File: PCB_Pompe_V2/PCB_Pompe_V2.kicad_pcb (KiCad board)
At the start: 2 copper layers, 199 parts, among them J1 Conn_01x04_Female, J10 Conn_01x03_Female, J11 Conn_01x03_Female, J12 Conn_01x03_Female, J13 Conn_01x05_Female, J14 Conn_01x03_Female, J15 Conn_01x03_Female, J16 Conn_01x03_Female, J17 Conn_01x03_Female, J18 Conn_01x03_Female, J19 Conn_01x03_Female, J2 Conn_01x04_Female, J3 Conn_01x03_Female, J4 Conn_01x03_Female, J5 Conn_01x03_Female, J6 Conn_01x03_Female, J7 Conn_01x03_Female, J8 Conn_01x02_Male, J9 Conn_01x03_Female, Q1 DMN10H700S, Q10 DMN10H700S, Q11 DMN10H700S, Q12 DMN10H700S, Q13 DMN10H700S, Q14 DMN10H700S, Q15 DMN10H700S, Q16 DMN10H700S, Q17 DMN10H700S, Q18 DMN10H700S, Q19 DMN10H700S, Q2 DMN10H700S, Q20 DMN10H700S, Q21 DMN10H700S, Q22 DMN10H700S, Q23 DMN10H700S, Q24 DMN10H700S, Q25 DMN10H700S, Q26 DMN10H700S, Q27 DMN10H700S, Q28 DMN10H700S, Q29 DMN10H700S, Q3 DMN10H700S, Q30 DMN10H700S, Q4 DMN10H700S, Q5 DMN10H700S, Q6 DMN10H700S, Q7 DMN10H700S, Q8 DMN10H700S, Q9 DMN10H700S, SW1 SW_Push, U1 SN65HVD232, U2 STM32F302C6Tx, U3 NCP1117-3.3_SOT223, Y1 8MHz

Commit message: change connector and some final touch
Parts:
- moved J8 120.9 mm to (184.2, 97.2), turned to 270 degrees
- moved H2 115.8 mm to (186.8, 129.8)
- moved C10 110.1 mm to (173.5, 100.0), turned to 90 degrees
- moved J13 104.0 mm to (158.5, 92.5), turned to 90 degrees
- moved R26 101.8 mm to (165.2, 76.5), turned to 270 degrees
- moved D26 98.1 mm to (165.2, 80.2), turned to 270 degrees
- moved J9 94.8 mm to (159.3, 78.0), turned to 180 degrees
- moved D28 94.6 mm to (157.0, 82.5), turned to 180 degrees
- moved D27 93.8 mm to (153.5, 80.5), turned to 270 degrees
- moved R51 92.7 mm to (181.5, 131.5), turned to 90 degrees
- moved Q11 90.2 mm to (162.5, 85.8), turned to 180 degrees
- moved R31 89.0 mm to (127.5, 118.5), turned to 90 degrees
- moved R50 88.1 mm to (169.8, 131.5), turned to 90 degrees
- moved J16 88.0 mm to (175.5, 130.0)
- moved D25 87.8 mm to (161.8, 82.5), turned to 180 degrees
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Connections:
- Y1 pad 1: Net-(C1-Pad1) -> Net-(C2-Pad1)
- Y1 pad 3: GND -> Net-(C1-Pad1)
- Y1 pad 4: Net-(C2-Pad1) -> GND
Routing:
- net +3V3: track 0.00 -> 125.4 mm
- net CANH: track 0.00 -> 62.7 mm
- net P1: track 0.00 -> 53.4 mm, vias 0 -> 2
- net P8: track 0.00 -> 49.5 mm, vias 0 -> 2
- net V1: track 0.00 -> 47.6 mm, vias 0 -> 2
- net V10: track 0.00 -> 45.0 mm, vias 0 -> 2
- net CANL: track 0.00 -> 41.0 mm, vias 0 -> 2
- net P10: track 0.00 -> 39.4 mm, vias 0 -> 2
- net P14: track 0.00 -> 39.0 mm
- net P2: track 0.00 -> 38.9 mm, vias 0 -> 2
- net V12: track 0.00 -> 38.1 mm, vias 0 -> 2
- net V6: track 0.00 -> 35.4 mm
- net +5V: track 0.00 -> 35.2 mm
- net V2: track 0.00 -> 34.2 mm, vias 0 -> 2
- net V3: track 0.00 -> 34.1 mm, vias 0 -> 2
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- added copper zone on F.Cu, net +5VP
- added copper zone on In1.Cu, net +5VP
- added copper zone on B.Cu, net GND
- added copper zone on F.Cu, net GND
- added copper zone on In2.Cu, net GND
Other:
- board outline added: 89.8 x 59.2 mm
- copper layers 2 -> 4

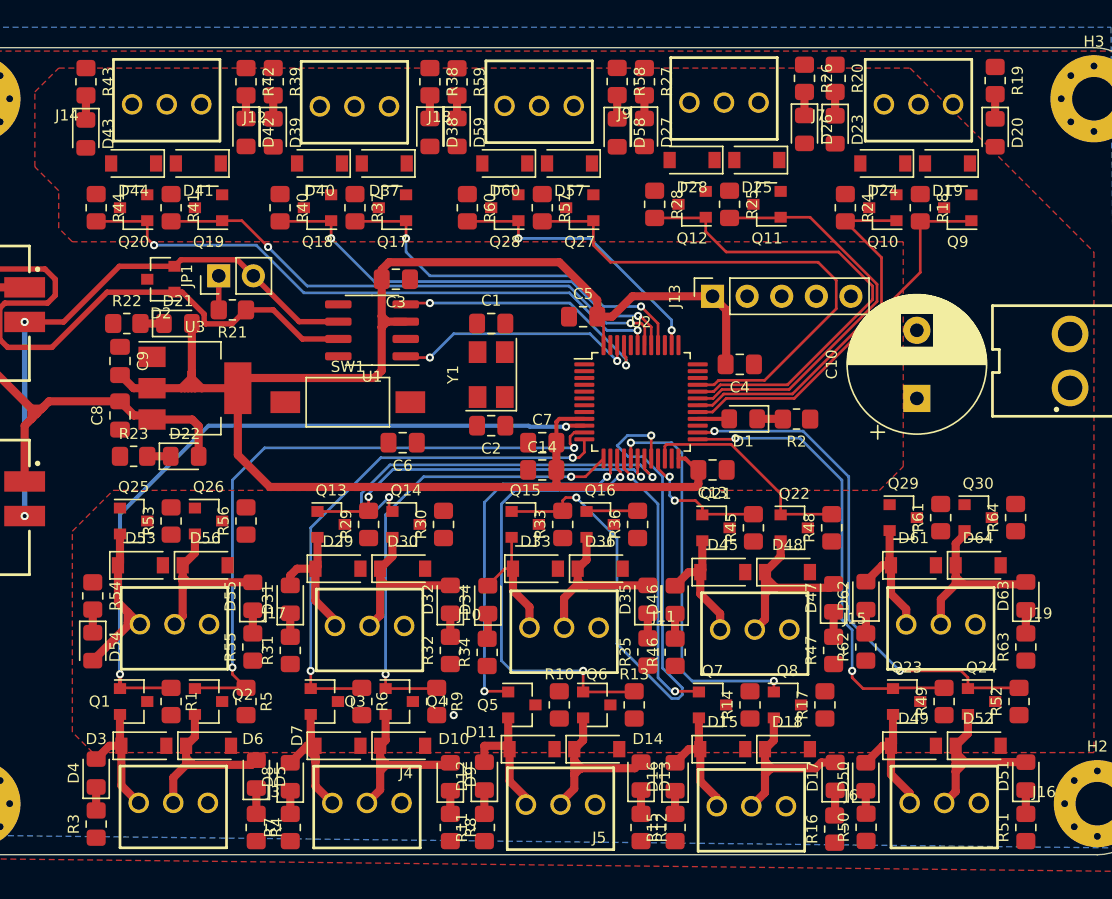
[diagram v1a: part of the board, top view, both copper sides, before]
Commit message: esp32 pas fini + silkscreen  IO ok
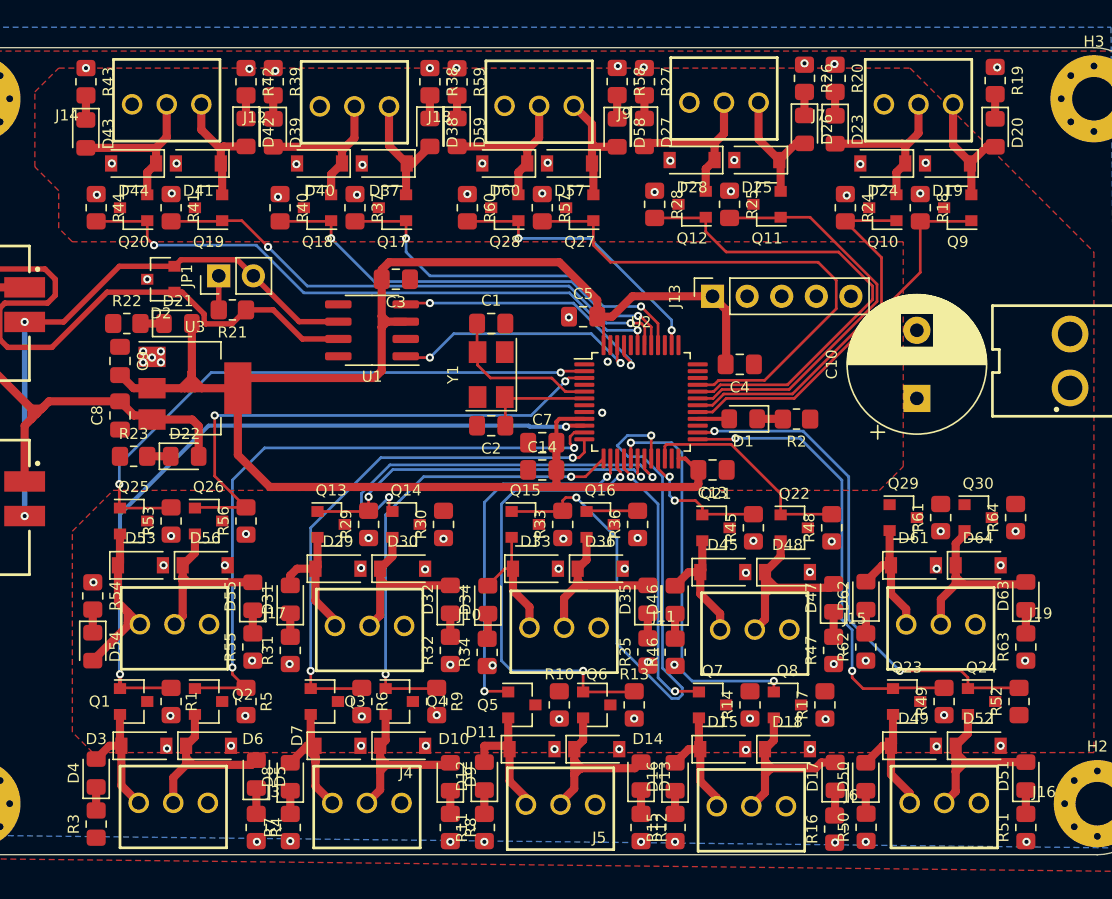
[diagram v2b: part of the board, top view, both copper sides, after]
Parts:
- removed C6: 1u, Capacitor_SMD:C_0805_2012Metric_Pad1.18x1.45mm_HandSolder
- removed SW1: SW_Push, Button_Switch_SMD:SW_SPST_FSMSM
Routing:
- net P13: track 0.00 -> 44.0 mm, vias 0 -> 2
- net V13: track 0.00 -> 39.7 mm, vias 0 -> 2
- net OUT_V5: track 0.00 -> 12.5 mm
- net OUT_V14: track 0.00 -> 12.4 mm
- net OUT_V10: track 0.00 -> 12.4 mm
- net OUT_V9: track 0.00 -> 12.4 mm
- net OUT_V6: track 0.00 -> 12.3 mm
- net Net-(C1-Pad1): track 0.00 -> 11.7 mm
- net OUT_P5: track 0.00 -> 9.55 mm
- net OUT_P6: track 0.00 -> 9.55 mm
- net OUT_P9: track 0.00 -> 9.27 mm
- net OUT_P10: track 0.00 -> 9.21 mm
- net OUT_P14: track 0.00 -> 9.07 mm
- net Net-(C2-Pad1): track 0.00 -> 7.99 mm
- net TXCAN: track 18.3 -> 18.9 mm
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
